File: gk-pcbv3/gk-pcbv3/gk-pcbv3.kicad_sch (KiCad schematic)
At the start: 83 parts, among them J1 USB_C_Receptacle_USB2.0, J10 Barrel_Jack_Switch, J12 Conn_01x02, J2 Conn_01x02, J8 Conn_ARM_JTAG_SWD_10, U1 WE-TVS-82400102, U10 MAX17048, U13 LTC3536xMSE, U15 MAX40203AUK, U16 MAX40203AUK, U2 MCP73831-2-OT, U3 AP62300WU

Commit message: v3 board
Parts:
- removed C14, C15, C16, C17, C18, C19, C20, C21, C22, C23, C24, C25, C26, C27, C28, C29, C30, C31, C34, C4, C75, C76: 100n, Capacitor_SMD:C_0603_1608Metric, symbol Device:C
- removed C3: 10u, Capacitor_SMD:C_0805_2012Metric, symbol Device:C
- removed C32: 4.7u, Capacitor_SMD:C_0805_2012Metric, symbol Device:C
- removed C33: 1u, Capacitor_SMD:C_0805_2012Metric, symbol Device:C
- removed C5: 10-100p, Capacitor_SMD:C_0603_1608Metric, symbol Device:C
- removed C6, C7, C87: 22u, Capacitor_SMD:C_0805_2012Metric, symbol Device:C
- removed C85: 47p, Capacitor_SMD:C_0603_1608Metric, symbol Device:C
- removed C86: 220p, Capacitor_SMD:C_0603_1608Metric, symbol Device:C
- removed D5: D, Diode_SMD:D_SOD-128, symbol Device:D
- removed D6: D_TVS, Diode_SMD:D_SMA, symbol Device:D_TVS
- removed J10: Barrel_Jack_Switch, Connector_BarrelJack:BarrelJack_Horizontal, symbol Connector:Barrel_Jack_Switch
- removed J12: Conn_01x02, Connector_PinHeader_2.54mm:PinHeader_1x02_P2.54mm_Vertical, symbol Connector_Generic:Conn_01x02
- removed L1: 3.3u, Inductor_SMD:L_7.3x7.3_H4.5, symbol Device:L
- removed L4: 4.7u, Inductor_SMD:L_7.3x7.3_H4.5, symbol Device:L
- removed R4: 31.6k, Resistor_SMD:R_0603_1608Metric, symbol Device:R
- removed R5, R72: 10k, Resistor_SMD:R_0603_1608Metric, symbol Device:R
- removed R52, R53, R54, R55: 100k, Resistor_SMD:R_0603_1608Metric, symbol Device:R
- removed R74: 1M, Resistor_SMD:R_0603_1608Metric, symbol Device:R
- removed R75: 221k, Resistor_SMD:R_0603_1608Metric, symbol Device:R
- removed R76: 6.49k, Resistor_SMD:R_0603_1608Metric, symbol Device:R
- removed R77: 49.9k, Resistor_SMD:R_0603_1608Metric, symbol Device:R
- removed R79: 0R / 1m-5m, Resistor_SMD:R_2512_6332Metric, symbol Device:R
- removed U13: LTC3536xMSE, Package_SO:MSOP-12-1EP_3x4mm_P0.65mm_EP1.65x2.85mm, symbol gk-syms:LTC3536xMSE
- removed U3: AP62300WU, Package_TO_SOT_SMD:TSOT-23-6, symbol Regulator_Switching:AP62300WU
- added D5: LED, LED_SMD:LED_0603_1608Metric, symbol Device:LED
- added J14: USB_A, Connector_USB:USB_A_Molex_67643_Horizontal, symbol Connector:USB_A
- added U23: WE-TVS-82400102, Package_TO_SOT_SMD:SOT-23-6, symbol Power_Protection:WE-TVS-82400102
- added U24: TPS2051CDBV, Package_TO_SOT_SMD:SOT-23-5, symbol Power_Management:TPS2051CDBV
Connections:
- net GND: now also J14.4 (GND), J14.5 (Shield), U23.2, U24.2 (GND)
- net VREGIN: no longer R73.1
- net I2C4_SCL renamed I2C2_SCL
- net I2C4_SDA renamed I2C2_SDA
- net VREG_PWM renamed +5V
- net +5V: now also U24.4 (EN), U24.5 (IN)
- new net: D5.1 (K), U24.3 (~{FLT})
- new net: D5.2 (A), R73.1
- new net: J14.1 (VBUS), U23.5, U24.1 (OUT)
- new net USB_HOST_D_N: J14.2 (D-), U23.3, U23.4
- new net USB_HOST_D_P: J14.3 (D+), U23.1, U23.6
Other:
- added sheet MCUB (mcub.kicad_sch)
- added sheet Power (power.kicad_sch)
- added sheet Wifi (wifi.kicad_sch)
- note removed: "Alternative 12V DC barrel jack input"
- note removed: "Connect VREG_PWM to open drain on MCU. Drive low for high current PWM mode else leave high. Use, e.g. for soft sleep with screen/wifi off"
- note removed: "MCU bypass caps"
- note removed: "VDDA Caps"
- note removed: "VDDSMPS Cap"

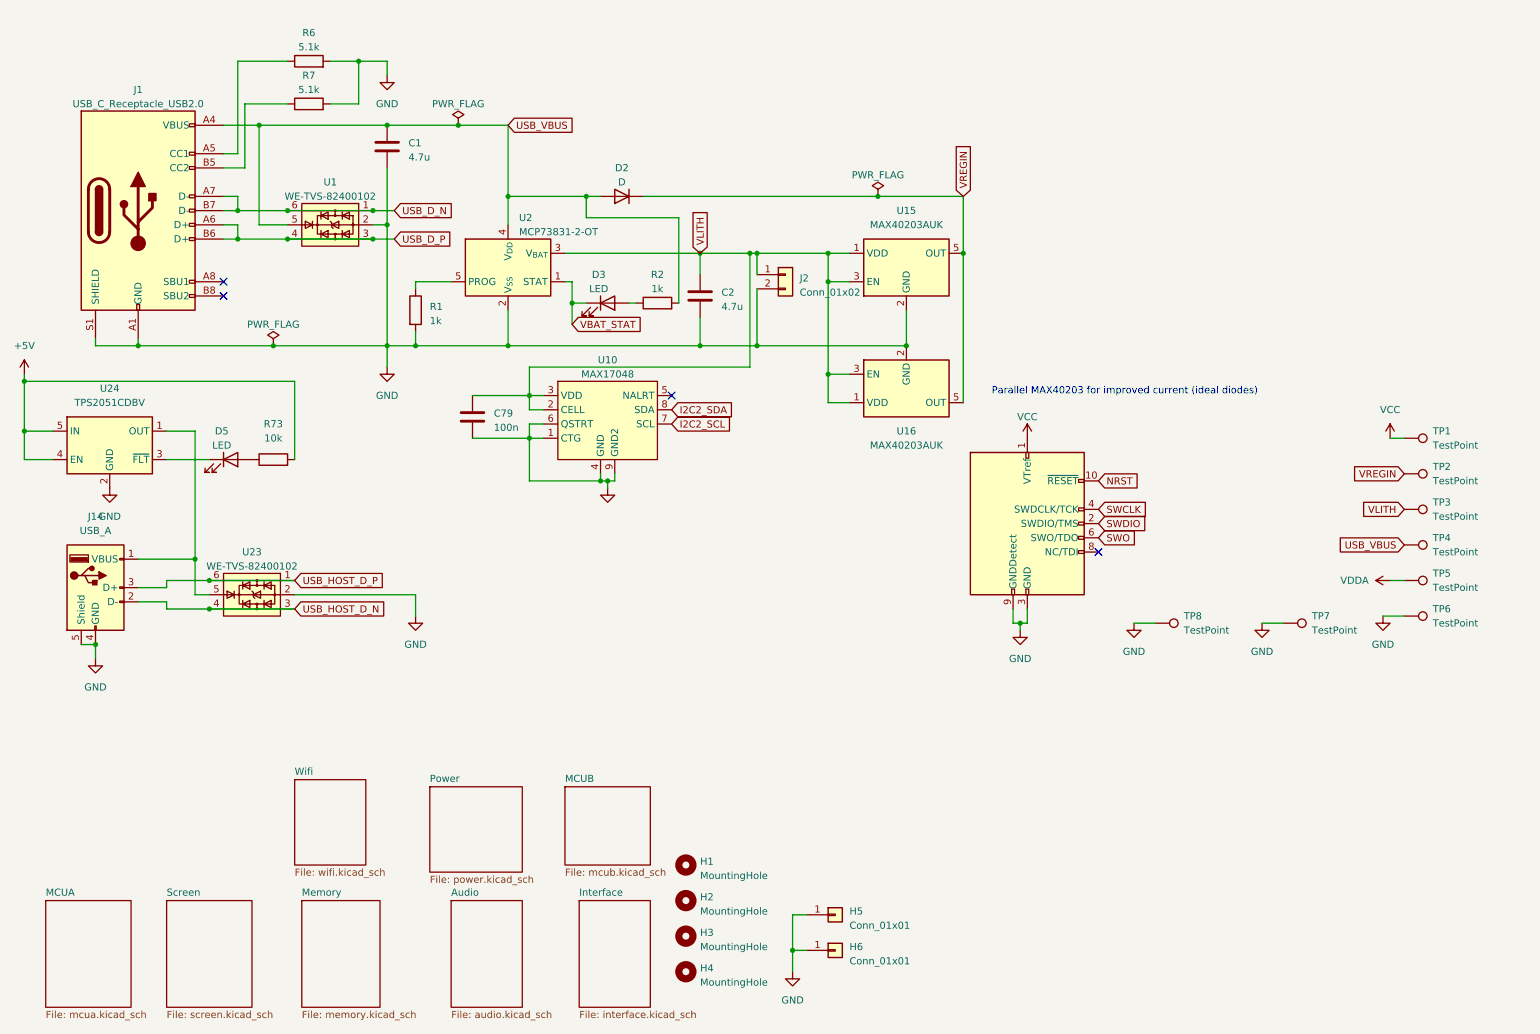
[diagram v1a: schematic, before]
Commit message: redesign for better signal integrity
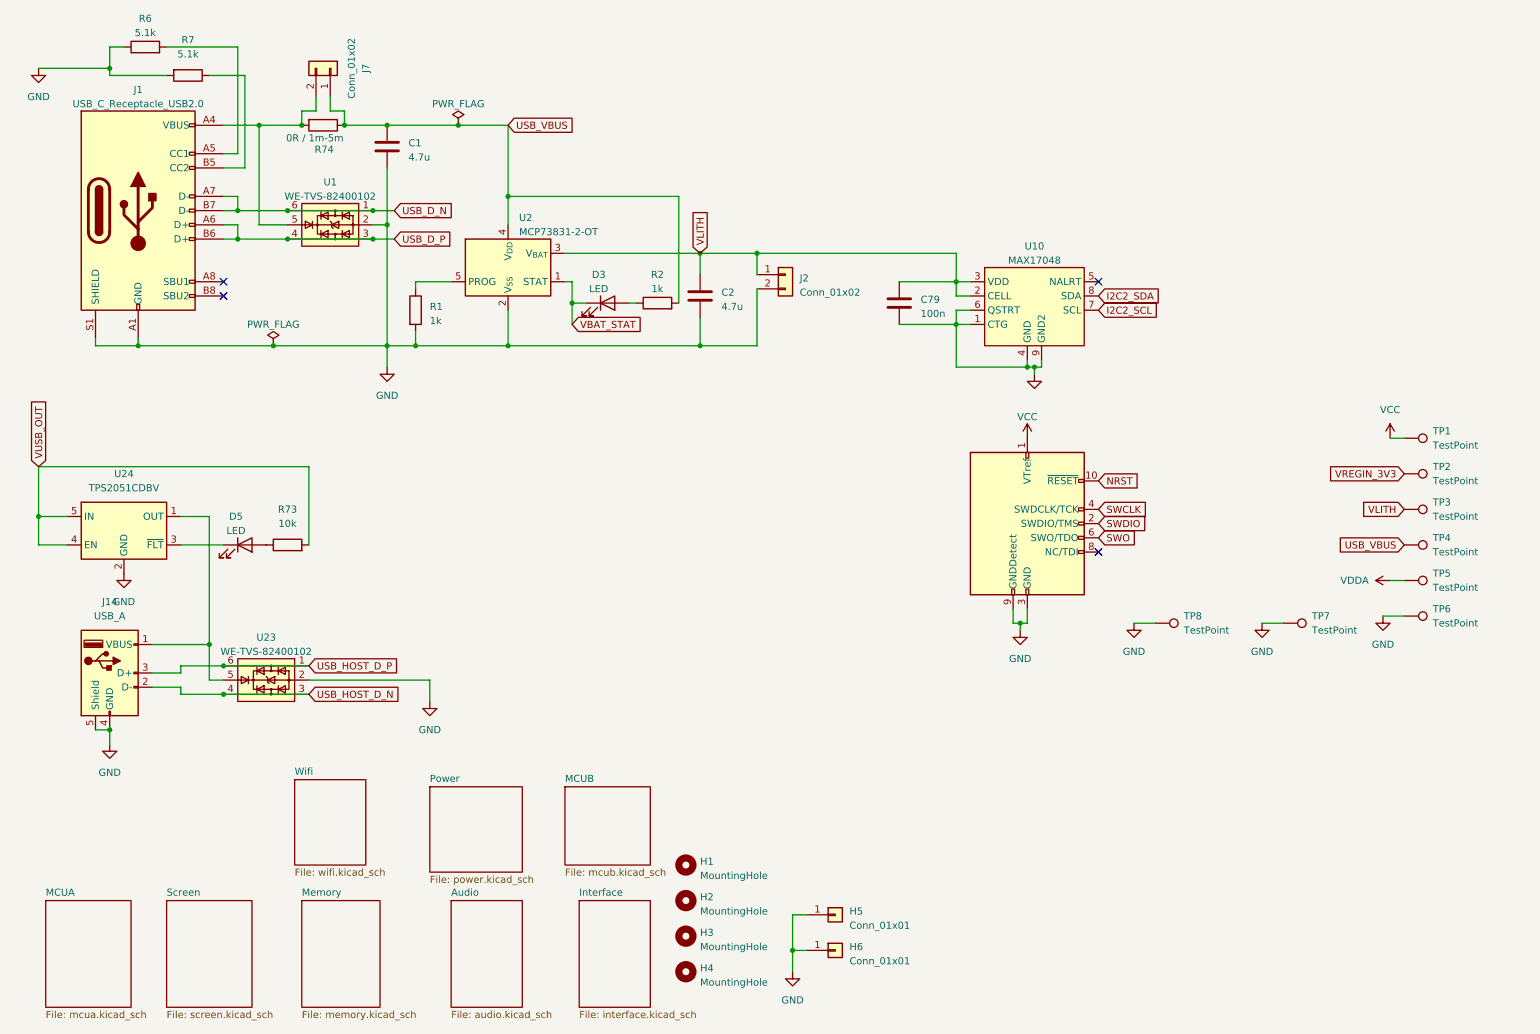
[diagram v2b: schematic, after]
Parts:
- removed D2: D, Diode_SMD:D_SOD-128, symbol Device:D
- removed U15, U16: MAX40203AUK, Package_TO_SOT_SMD:SOT-23-5, symbol Analog_Switch:MAX40200AUK
- added J7: Conn_01x02, Connector_PinHeader_2.54mm:PinHeader_1x02_P2.54mm_Vertical, symbol Connector_Generic:Conn_01x02
- added R74: 0R / 1m-5m, Resistor_SMD:R_2512_6332Metric, symbol Device:R
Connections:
- net GND: now also R6.1; no longer R6.2
- net USB_VBUS: now also J7.1 (Pin_1), R74.1; no longer J1.A4 (VBUS), J1.A9 (VBUS), J1.B4 (VBUS), J1.B9 (VBUS), U1.5
- net at J1.A5 (CC1): now also R6.2; no longer R6.1
- net +5V renamed VUSB_OUT
- net VREGIN renamed VREGIN_3V3
- new net: J1.A4 (VBUS), J1.A9 (VBUS), J1.B4 (VBUS), J1.B9 (VBUS), J7.2 (Pin_2), R74.2, U1.5
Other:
- note removed: "Parallel MAX40203 for improved current (ideal diodes)"
- moved on the sheet: C79, D5, J14, R6, R7, R73, U10, U23, U24

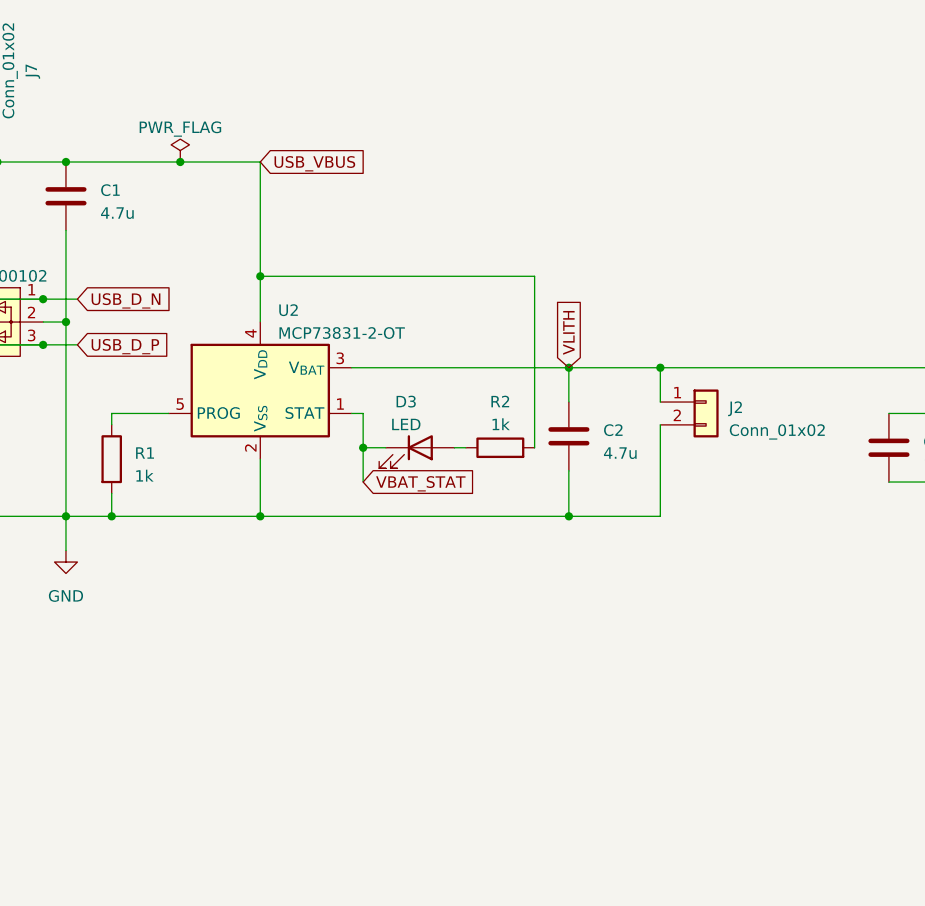
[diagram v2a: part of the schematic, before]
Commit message: Route top end of board Remove vbat stat LED
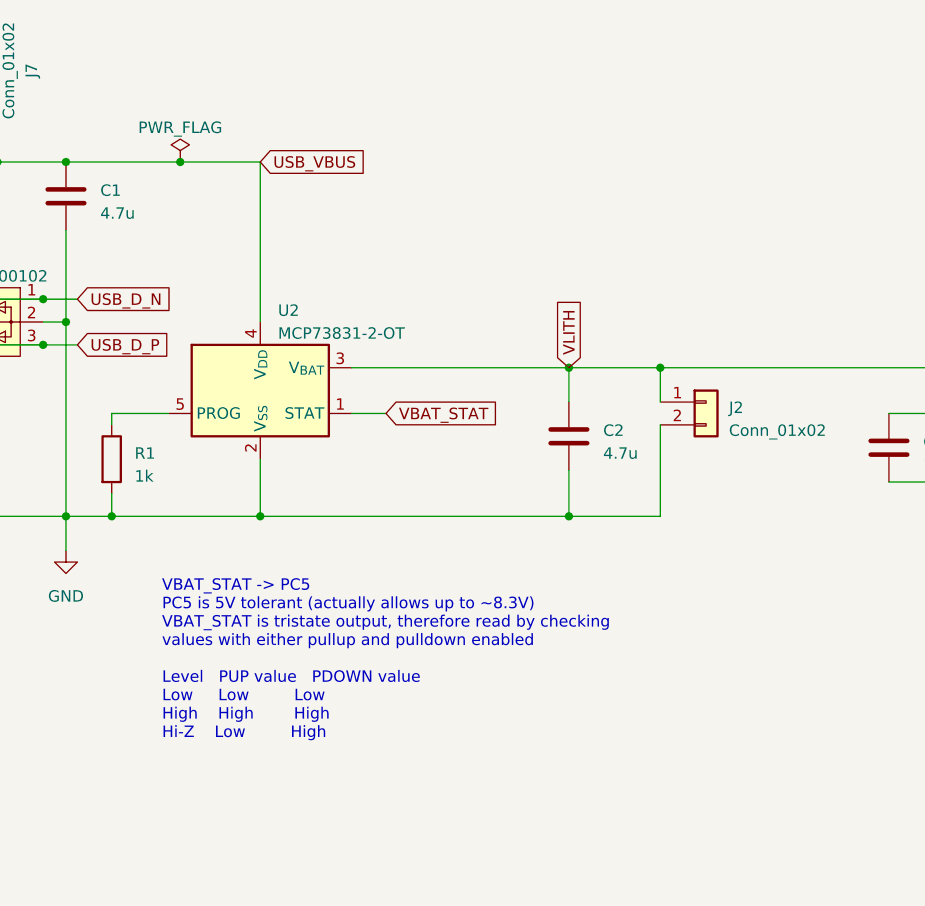
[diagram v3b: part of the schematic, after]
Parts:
- removed D3: LED, LED_SMD:LED_0603_1608Metric, symbol Device:LED
- removed R2: 1k, Resistor_SMD:R_0603_1608Metric, symbol Device:R
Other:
- note added: "VBAT_STAT -> PC5 PC5 is 5V tolerant (actually allows up to ~8.3V) VBAT_STAT is tristate output, therefore read by checking values with either pullup and pulldown enabled Level PUP value PDOWN value Low Low Low High High High Hi-Z Low High"
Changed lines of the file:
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@@
 	)
 	(junction
-		(at 102.87 45.72)
-		(diameter 0)
-		(color 0 0 0 0)
-	)
-	(junction
 		(at 81.28 50.8)
 		(diameter 0)
@@
 	)
 	(junction
-		(at 114.3 64.77)
-		(diameter 0)
-		(color 0 0 0 0)
-	)
-	(junction
 		(at 147.32 55.88)
 		(diameter 0)
@@
 	(wire
 		(pts
-			(xy 114.3 64.77) (xy 114.3 60.96)
-		)
-		(stroke
-			(width 0)
-			(type default)
-		)
-	)
-	(wire
-		(pts
 			(xy 58.42 50.8) (xy 63.5 50.8)
 		)
@@
 	(wire
 		(pts
-			(xy 102.87 45.72) (xy 102.87 33.02)
+			(xy 102.87 33.02) (xy 102.87 50.8)
 		)
 		(stroke
@@
 	(wire
 		(pts
-			(xy 133.35 45.72) (xy 133.35 64.77)
-		)
-		(stroke
-			(width 0)
-			(type default)
-		)
-	)
-	(wire
-		(pts
 			(xy 214.63 121.92) (xy 218.44 121.92)
 		)
@@
 	(wire
 		(pts
-			(xy 114.3 60.96) (xy 113.03 60.96)
+			(xy 116.84 60.96) (xy 113.03 60.96)
 		)
 		(stroke
@@
 	(wire
 		(pts
-			(xy 124.46 64.77) (xy 125.73 64.77)
-		)
-		(stroke
-			(width 0)
-			(type default)
-		)
-	)
-	(wire
-		(pts
 			(xy 49.53 102.87) (xy 49.53 125.73)
 		)
@@
 	(wire
 		(pts
-			(xy 116.84 64.77) (xy 114.3 64.77)
-		)
-		(stroke
-			(width 0)
-			(type default)
-		)
-	)
-	(wire
-		(pts
-			(xy 114.3 64.77) (xy 114.3 68.58)
-		)
-		(stroke
-			(width 0)
-			(type default)
-		)
-	)
-	(wire
-		(pts
 			(xy 260.35 114.3) (xy 262.89 114.3)
 		)
@@
 	(wire
 		(pts
-			(xy 102.87 50.8) (xy 102.87 45.72)
-		)
-		(stroke
-			(width 0)
-			(type default)
-		)
-	)
-	(wire
-		(pts
 			(xy 52.07 48.26) (xy 54.61 48.26)
 		)
@@
 	(wire
 		(pts
-			(xy 102.87 45.72) (xy 133.35 45.72)
-		)
-		(stroke
-			(width 0)
-			(type default)
-		)
-	)
-	(wire
-		(pts
 			(xy 194.31 121.92) (xy 194.31 123.19)
 		)
@@
 		)
 	)
+	(text "VBAT_STAT -> PC5\nPC5 is 5V tolerant (actually allows up to ~8.3V)\nVBAT_STAT is tristate output, therefore read by checking\nvalues with either pullup and pulldown enabled\n\nLevel   PUP value   PDOWN value\nLow     Low         Low\nHigh    High        High\nHi-Z    Low         High"
+		(exclude_from_sim no)
+		(at 91.948 88.392 0)
+		(effects
+			(font
+				(face "Courier New")
+				(size 1.27 1.27)
+			)
+			(justify left)
+		)
+	)
 	(global_label "USB_D_P"
 		(shape input)
@@
 	(global_label "VBAT_STAT"
 		(shape input)
-		(at 114.3 68.58 0)
+		(at 116.84 60.96 0)
 		(fields_autoplaced yes)
 		(effects
@@
 		)
 		(property "Intersheetrefs" "${INTERSHEET_REFS}"
-			(at 126.8215 68.58 0)
+			(at 129.3615 60.96 0)
 			(effects
 				(font
@@
 	)
 	(symbol
-		(lib_id "Device:LED")
-		(at 120.65 64.77 0)
-		(unit 1)
-		(exclude_from_sim no)
-		(in_bom yes)
-		(on_board yes)
-		(dnp no)
-		(fields_autoplaced yes)
-		(property "Reference" "D3"
-			(at 119.0625 59.69 0)
-			(effects
-				(font
-					(size 1.27 1.27)
-				)
-			)
-		)
-		(property "Value" "LED"
-			(at 119.0625 62.23 0)
-			(effects
-				(font
-					(size 1.27 1.27)
-				)
-			)
-		)
-		(property "Footprint" "LED_SMD:LED_0603_1608Metric"
-			(at 120.65 64.77 0)
-			(effects
-				(font
-					(size 1.27 1.27)
-				)
-				(hide yes)
-			)
-		)
-		(property "Datasheet" "~"
-			(at 120.65 64.77 0)
-			(effects
-				(font
-					(size 1.27 1.27)
-				)
-				(hide yes)
-			)
-		)
-		(property "Description" ""
-			(at 120.65 64.77 0)
-			(effects
-				(font
-					(size 1.27 1.27)
-				)
-				(hide yes)
-			)
-		)
-		(pin "1"
-		)
-		(pin "2"
-		)
-		(instances
-			(project "gk-pcbv2"
-				(path "/08730ac6-6084-459f-bdf1-86b322355ede"
-					(reference "D3")
-					(unit 1)
-				)
-			)
-		)
-	)
-	(symbol
 		(lib_id "Device:R")
 		(at 86.36 66.04 0)
@@
 					(unit 1)
 				)
-			)
-		)
-	)
-	(symbol
-		(lib_id "Device:R")
-		(at 129.54 64.77 90)
-		(unit 1)
-		(exclude_from_sim no)
-		(in_bom yes)
-		(on_board yes)
-		(dnp no)
-		(fields_autoplaced yes)
-		(property "Reference" "R2"
-			(at 129.54 59.69 90)
-			(effects
-				(font
-					(size 1.27 1.27)
-				)
-			)
-		)
-		(property "Value" "1k"
-			(at 129.54 62.23 90)
-			(effects
-				(font
-					(size 1.27 1.27)
-				)
-			)
-		)
-		(property "Footprint" "Resistor_SMD:R_0603_1608Metric"
-			(at 129.54 66.548 90)
-			(effects
-				(font
-					(size 1.27 1.27)
-				)
-				(hide yes)
-			)
-		)
-		(property "Datasheet" "~"
-			(at 129.54 64.77 0)
-			(effects
-				(font
-					(size 1.27 1.27)
-				)
-				(hide yes)
-			)
-		)
-		(property "Description" ""
-			(at 129.54 64.77 0)
-			(effects
-				(font
-					(size 1.27 1.27)
-				)
-				(hide yes)
-			)
-		)
-		(pin "1"
-		)
-		(pin "2"
-		)
-		(instances
-			(project "gk-pcbv2"
-				(path "/08730ac6-6084-459f-bdf1-86b322355ede"
-					(reference "R2")
-					(unit 1)
-				)
